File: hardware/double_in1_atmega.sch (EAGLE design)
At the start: 37 parts, among them IC1 MEGA8-AI, J1 AVR-ISP-6PINAVR-ISP-6PIN-SMAL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

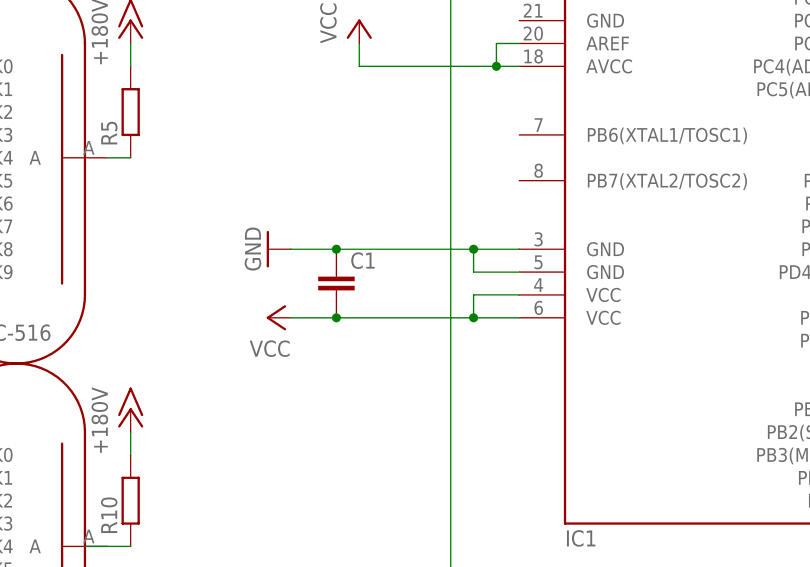
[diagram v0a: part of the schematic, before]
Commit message: [PCB] rev1; Change resistors size, center ATMEGA8, make slots for nixie alignment, minor changes
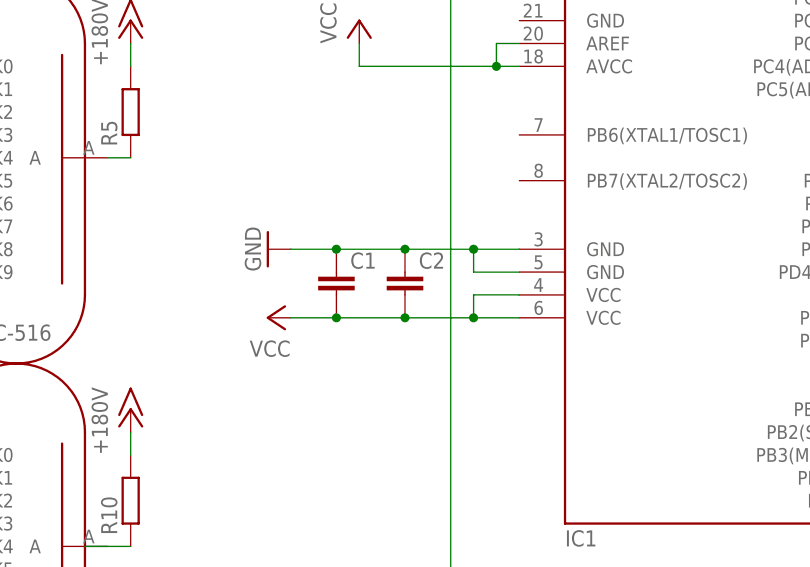
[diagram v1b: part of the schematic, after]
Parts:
- added C2: (no value), eagle-ltspice:C
- R1, R11, R2, R3, R4, R6, R7, R8, R9: device resistor:R-EU_R0402 -> resistor:R-EU_R0603
- R10, R5: device resistor:R-EU_R0402 -> rcl:R-EU_M1206
- U$1, U$2: device LC-516:LC-516 -> LC-516_play:LC-516
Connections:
- net GND: now also C2.1
- net VCC: now also C2.2

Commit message: generate gerber for jlpcb
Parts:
- added GOLD_ORB_SM1: OSHWLOGOLOGO5MM, oshw:OSHWLOGOLOGO5MM
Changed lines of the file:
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@@
 <?xml version="1.0" encoding="utf-8"?>
 <!DOCTYPE eagle SYSTEM "eagle.dtd">
-<eagle version="8.7.0">
+<eagle version="9.1.0">
 <drawing>
 <settings>
@@
 <layer number="48" name="Document" color="7" fill="1" visible="no" active="no"/>
 <layer number="49" name="Reference" color="7" fill="1" visible="no" active="no"/>
+<layer number="50" name="dxf" color="7" fill="1" visible="no" active="no"/>
 <layer number="51" name="tDocu" color="7" fill="1" visible="no" active="no"/>
 <layer number="52" name="bDocu" color="7" fill="1" visible="no" active="no"/>
+<layer number="53" name="tGND_GNDA" color="7" fill="9" visible="no" active="no"/>
+<layer number="54" name="bGND_GNDA" color="1" fill="9" visible="no" active="no"/>
+<layer number="56" name="wert" color="7" fill="1" visible="no" active="no"/>
+<layer number="90" name="Modules" color="5" fill="1" visible="yes" active="yes"/>
 <layer number="91" name="Nets" color="2" fill="1" visible="yes" active="yes"/>
 <layer number="92" name="Busses" color="1" fill="1" visible="yes" active="yes"/>
@@
 <layer number="98" name="Guide" color="6" fill="1" visible="yes" active="yes"/>
 <layer number="99" name="SpiceOrder" color="5" fill="1" visible="yes" active="yes"/>
+<layer number="100" name="Muster" color="7" fill="1" visible="no" active="no"/>
+<layer number="101" name="Patch_Top" color="12" fill="4" visible="yes" active="yes"/>
+<layer number="102" name="Vscore" color="7" fill="1" visible="yes" active="yes"/>
+<layer number="103" name="tMap" color="7" fill="1" visible="yes" active="yes"/>
+<layer number="104" name="Name" color="7" fill="1" visible="yes" active="yes"/>
+<layer number="105" name="tPlate" color="7" fill="1" visible="yes" active="yes"/>
+<layer number="106" name="bPlate" color="7" fill="1" visible="yes" active="yes"/>
+<layer number="107" name="Crop" color="7" fill="1" visible="yes" active="yes"/>
+<layer number="116" name="Patch_BOT" color="9" fill="4" visible="yes" active="yes"/>
+<layer number="121" name="_tsilk" color="7" fill="1" visible="yes" active="yes"/>
+<layer number="122" name="_bsilk" color="7" fill="1" visible="yes" active="yes"/>
+<layer number="125" name="_tNames" color="7" fill="1" visible="yes" active="yes"/>
+<layer number="144" name="Drill_legend" color="7" fill="1" visible="yes" active="yes"/>
+<layer number="151" name="HeatSink" color="7" fill="1" visible="yes" active="yes"/>
+<layer number="200" name="200bmp" color="1" fill="10" visible="yes" active="yes"/>
+<layer number="201" name="201bmp" color="2" fill="1" visible="no" active="no"/>
+<layer number="202" name="202bmp" color="3" fill="1" visible="no" active="no"/>
+<layer number="203" name="203bmp" color="4" fill="10" visible="yes" active="yes"/>
+<layer number="204" name="204bmp" color="5" fill="10" visible="yes" active="yes"/>
+<layer number="205" name="205bmp" color="6" fill="10" visible="yes" active="yes"/>
+<layer number="206" name="206bmp" color="7" fill="10" visible="yes" active="yes"/>
+<layer number="207" name="207bmp" color="8" fill="10" visible="yes" active="yes"/>
+<layer number="208" name="208bmp" color="9" fill="10" visible="yes" active="yes"/>
+<layer number="209" name="209bmp" color="7" fill="1" visible="yes" active="yes"/>
+<layer number="210" name="210bmp" color="7" fill="1" visible="yes" active="yes"/>
+<layer number="211" name="211bmp" color="7" fill="1" visible="yes" active="yes"/>
+<layer number="212" name="212bmp" color="7" fill="1" visible="yes" active="yes"/>
+<layer number="213" name="213bmp" color="7" fill="1" visible="yes" active="yes"/>
+<layer number="214" name="214bmp" color="7" fill="1" visible="yes" active="yes"/>
+<layer number="215" name="215bmp" color="7" fill="1" visible="yes" active="yes"/>
+<layer number="216" name="216bmp" color="7" fill="1" visible="yes" active="yes"/>
+<layer number="250" name="Descript" color="3" fill="1" visible="no" active="no"/>
+<layer number="251" name="SMDround" color="12" fill="11" visible="no" active="no"/>
+<layer number="254" name="cooling" color="7" fill="1" visible="yes" active="yes"/>
 </layers>
 <schematic xreflabel="%F%N/%S.%C%R" xrefpart="/%S.%C%R">
@@
 <part name="U$2" library="LC-516_play" deviceset="LC-516" device=""/>
 <part name="C2" library="eagle-ltspice" library_urn="urn:adsk.eagle:library:217" deviceset="C" device="" package3d_urn="urn:adsk.eagle:package:13265/1"/>
+<part name="GOLD_ORB_SM1" library="oshw" deviceset="OSHWLOGO" device="LOGO5MM"/>
 </parts>
 <sheets>
@@
 <instance part="U$2" gate="G$1" x="35.56" y="10.16"/>
 <instance part="C2" gate="G$1" x="81.28" y="40.64"/>
+<instance part="GOLD_ORB_SM1" gate="G$1" x="12.7" y="91.44"/>
 </instances>
 <busses>
@@
 </drawing>
 <compatibility>
+<note version="6.3" minversion="6.2.2" severity="warning">
+Since Version 6.2.2 text objects can contain more than one line,
+which will not be processed correctly with this version.
+</note>
 <note version="8.2" severity="warning">
 Since Version 8.2, EAGLE supports online libraries. The ids
